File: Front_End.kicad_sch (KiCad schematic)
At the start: 40 parts, among them J6 Conn_01x03, J7 Conn_01x03, J8 Conn_01x03, J9 Conn_01x03

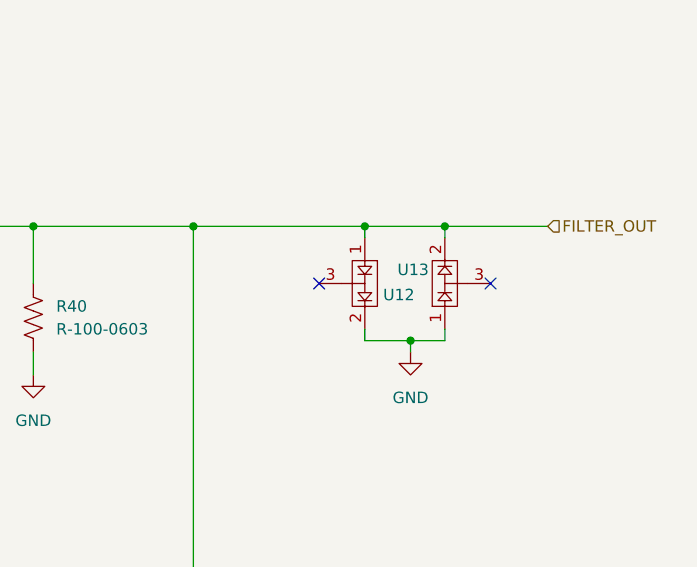
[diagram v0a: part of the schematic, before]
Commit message: Bring over ringof/dev: design + 3D + mechanical/viewer + CI (#58)
* throwaway: exercise design -> dev pipeline (safe to delete)

* Bring over ringof/dev (tranche 2, stage 1): design, library, 3D, board CI & docs

* Bring over ringof/dev (tranche 2, stage 2): mechanical enclosure + 3D viewer

* run_checks: hard-fail the 3D-model check regardless of ENFORCE

* Improved 3D viewer (#59)

* mechanical: give the end plates a Blue soldermask stackup

The end-plate PCBs had no physical stackup, so KiCad exported them with the
default green soldermask. Add a 2-layer stackup with front/back mask set to the
named "Blue" preset, summing to the existing 1.6 mm so board thickness / fit is
unchanged. This makes the plates export blue-dominant so the viewer's soldermask
recolour treats them the same as the main board.

* feat(viewer): part toggles, upright orientation, Turn Island navy, even lighting

Grow the mechanical fit-check viewer into an interactive, correctly-coloured one:

- Part toggles: show/hide enclosure, main board, front/rear end plate. Rebuilt on
  pinned three.js r148 (model-viewer has no per-node visibility API); a checkbox
  flips object.visible on each part's prefixed nodes. Libraries inlined via a
  runtime import map -- no bundler, fully offline.
- Upright orientation (180 deg roll), click-to-set-pivot, and a header showing the
  git hash and branch as links (new --repo-url, fed from the CI environment).
- Board colour: assemble_glb recolours the blue soldermask to the Turn Island navy
  (KiCad's "Blue" preset exports a brighter cornflower); detection targets only the
  matte, blue-dominant mask material. The material is identical on every face, so
  the viewer lighting is set to an orientation-independent rig (soft key + strong
  ambient + damped environment) so every face reads the same navy.
- Checkbox reload-sync: autocomplete="off" + re-apply each box's state on load so
  the model always matches the checkboxes after a refresh.

Colour is applied downstr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
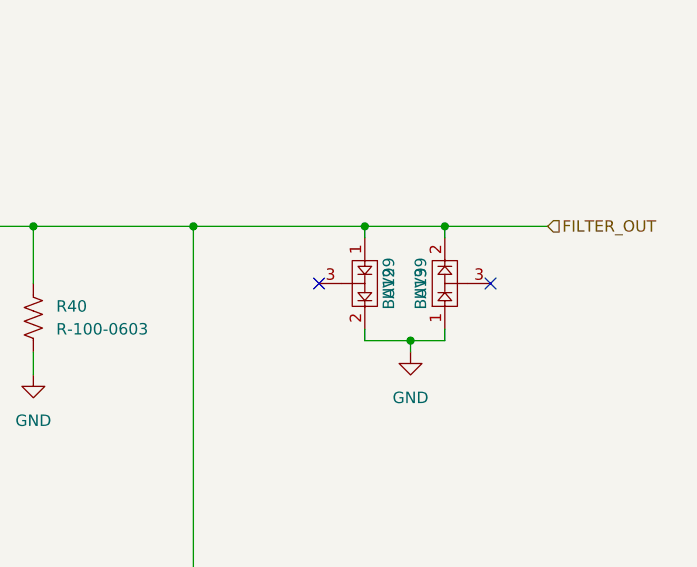
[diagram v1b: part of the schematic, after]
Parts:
- C48, C49, C50, C53, C54, C55, C56, C58, C59, C61: footprint TIS_Footprints:C_0603 -> Library:C_0603
- C51, C52, C57, C60: footprint TIS_Footprints:PAD_0603 -> Library:C_0603
- J6, J7, J8, J9: footprint TIS_Footprints:Pin_Header_Straight_1x03_Pitch2.54mm -> Library:Pin_Header_Straight_1x03_Pitch2.54mm
- L10, L11: footprint TIS_Footprints:Murata2U -> Library:Murata2U; LCSC Part # C2044072 -> C703706
- L12, L13, L14, L8, L9: footprint TIS_Footprints:Murata2U -> Library:Murata2U
- R28, R29, R30, R31, R32, R33, R34, R35, R36, R37, R38, R39, R40: footprint TIS_Footprints:PAD_0603 -> Library:PAD_0603
- U12, U13: value (none) -> BAV99; footprint TIS_Footprints:SOT-23 -> Library:SOT-23
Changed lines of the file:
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@@
 			)
 		)
-		(property "Footprint" "TIS_Footprints:PAD_0603"
+		(property "Footprint" "Library:PAD_0603"
 			(at 117.856 65.024 90)
 			(hide yes)
@@
 			)
 		)
-		(property "Footprint" "TIS_Footprints:PAD_0603"
+		(property "Footprint" "Library:C_0603"
 			(at 60.96 99.06 0)
 			(hide yes)
@@
 			)
 		)
-		(property "Footprint" "TIS_Footprints:Pin_Header_Straight_1x03_Pitch2.54mm"
+		(property "Footprint" "Library:Pin_Header_Straight_1x03_Pitch2.54mm"
 			(at 51.181 21.336 0)
 			(hide yes)
@@
 			)
 		)
-		(property "Footprint" "TIS_Footprints:PAD_0603"
+		(property "Footprint" "Library:PAD_0603"
 			(at 77.216 65.024 90)
 			(hide yes)
@@
 			)
 		)
-		(property "Footprint" "TIS_Footprints:C_0603"
+		(property "Footprint" "Library:C_0603"
 			(at 96.774 135.382 0)
 			(hide yes)
@@
 			)
 		)
-		(property "Footprint" "TIS_Footprints:Murata2U"
+		(property "Footprint" "Library:Murata2U"
 			(at 64.77 111.76 0)
 			(hide yes)
@@
 			)
 		)
-		(property "Footprint" "TIS_Footprints:Murata2U"
+		(property "Footprint" "Library:Murata2U"
 			(at 170.18 111.76 0)
 			(hide yes)
@@
 			)
 		)
-		(property "Footprint" "TIS_Footprints:C_0603"
+		(property "Footprint" "Library:C_0603"
 			(at 115.824 135.382 0)
 			(hide yes)
@@
 			)
 		)
-		(property "Footprint" "TIS_Footprints:C_0603"
+		(property "Footprint" "Library:C_0603"
 			(at 52.324 135.382 0)
 			(hide yes)
@@
 			)
 		)
-		(property "Footprint" "TIS_Footprints:PAD_0603"
+		(property "Footprint" "Library:PAD_0603"
 			(at 124.714 57.404 90)
 			(hide yes)
@@
 			)
 		)
-		(property "Footprint" "TIS_Footprints:PAD_0603"
+		(property "Footprint" "Library:PAD_0603"
 			(at 54.864 157.734 90)
 			(hide yes)
@@
 			)
 		)
-		(property "Footprint" "TIS_Footprints:PAD_0603"
+		(property "Footprint" "Library:PAD_0603"
 			(at 76.454 48.514 90)
 			(hide yes)
@@
 		)
 		(property "LCSC Part #" "C22962"
-			(at 76.2 49.53 0)
+			(at 76.2 49.53 90)
 			(hide yes)
 			(show_name no)
@@
 			)
 		)
-		(property "Footprint" "TIS_Footprints:PAD_0603"
+		(property "Footprint" "Library:PAD_0603"
 			(at 81.534 157.734 90)
 			(hide yes)
@@
 			)
 		)
-		(property "Footprint" "TIS_Footprints:C_0603"
+		(property "Footprint" "Library:C_0603"
 			(at 87.122 114.046 0)
 			(hide yes)
@@
 			)
 		)
-		(property "Footprint" "TIS_Footprints:Pin_Header_Straight_1x03_Pitch2.54mm"
+		(property "Footprint" "Library:Pin_Header_Straight_1x03_Pitch2.54mm"
 			(at 188.849 98.806 0)
 			(hide yes)
@@
 			)
 		)
-		(property "Footprint" "TIS_Footprints:PAD_0603"
+		(property "Footprint" "Library:C_0603"
 			(at 113.03 27.94 0)
 			(hide yes)
@@
 			)
 		)
-		(property "Footprint" "TIS_Footprints:C_0603"
+		(property "Footprint" "Library:C_0603"
 			(at 75.184 135.382 0)
 			(hide yes)
@@
 			)
 		)
-		(property "Footprint" "TIS_Footprints:PAD_0603"
+		(property "Footprint" "Library:PAD_0603"
 			(at 42.926 165.354 90)
 			(hide yes)
@@
 			)
 		)
-		(property "Footprint" "TIS_Footprints:Murata2U"
+		(property "Footprint" "Library:Murata2U"
 			(at 86.36 111.76 0)
 			(hide yes)
@@
 			)
 		)
-		(property "LCSC Part #" "C2044072"
+		(property "LCSC Part #" "C703706"
 			(at 86.487 113.538 0)
 			(hide yes)
@@
 		(dnp no)
 		(property "Reference" "U12"
-			(at 245.872 114.3 90)
+			(at 246.507 113.03 0)
 			(show_name no)
 			(do_not_autoplace no)
@@
 					(size 1.27 1.27)
 				)
-				(justify left)
 			)
 		)
-		(property "Value" ""
-			(at 246.38 114.3635 90)
+		(property "Value" "BAV99"
+			(at 246.507 113.03 0)
 			(show_name no)
 			(do_not_autoplace no)
@@
 					(size 1.27 1.27)
 				)
-				(justify left)
 			)
 		)
-		(property "Footprint" "TIS_Footprints:SOT-23"
+		(property "Footprint" "Library:SOT-23"
 			(at 248.412 112.903 0)
 			(hide yes)
@@
 			)
 		)
-		(property "Footprint" "TIS_Footprints:C_0603"
+		(property "Footprint" "Library:C_0603"
 			(at 33.782 48.006 0)
 			(hide yes)
@@
 		(dnp no)
 		(property "Reference" "U13"
-			(at 250.952 111.506 90)
+			(at 250.063 113.03 0)
 			(show_name no)
 			(do_not_autoplace no)
@@
 					(size 1.27 1.27)
 				)
-				(justify left)
 			)
 		)
-		(property "Value" ""
-			(at 250.19 114.2365 90)
+		(property "Value" "BAV99"
+			(at 250.063 113.03 0)
 			(show_name no)
 			(do_not_autoplace no)
@@
 					(size 1.27 1.27)
 				)
-				(justify left)
 			)
 		)
-		(property "Footprint" "TIS_Footprints:SOT-23"
+		(property "Footprint" "Library:SOT-23"
 			(at 248.158 113.157 0)
 			(hide yes)
@@
 			)
 		)
-		(property "Footprint" "TIS_Footprints:Pin_Header_Straight_1x03_Pitch2.54mm"
+		(property "Footprint" "Library:Pin_Header_Straight_1x03_Pitch2.54mm"
 			(at 48.641 98.806 0)
 			(hide yes)
@@
 			)
 		)
-		(property "Footprint" "TIS_Footprints:PAD_0603"
+		(property "Footprint" "Library:PAD_0603"
 			(at 117.094 48.514 90)
 			(hide yes)
@@
 		)
 		(property "LCSC Part #" "C22962"
-			(at 116.84 49.53 0)
+			(at 116.84 49.53 90)
 			(hide yes)
 			(show_name no)
@@
 			)
 		)
-		(property "Footprint" "TIS_Footprints:PAD_0603"
+		(property "Footprint" "Library:PAD_0603"
 			(at 208.026 117.094 90)
 			(hide yes)
@@
 			)
 		)
-		(property "Footprint" "TIS_Footprints:C_0603"
+		(property "Footprint" "Library:C_0603"
 			(at 129.032 114.046 0)
 			(hide yes)
@@
 			)
 		)
-		(property "Footprint" "TIS_Footprints:C_0603"
+		(property "Footprint" "Library:C_0603"
 			(at 35.052 161.036 0)
 			(hide yes)
@@
 			)
 		)
-		(property "Footprint" "TIS_Footprints:C_0603"
+		(property "Footprint" "Library:C_0603"
 			(at 107.442 114.046 0)
 			(hide yes)
@@
 			)
 		)
-		(property "Footprint" "TIS_Footprints:Murata2U"
+		(property "Footprint" "Library:Murata2U"
 			(at 64.77 73.66 0)
 			(hide yes)
@@
 			)
 		)
-		(property "Footprint" "TIS_Footprints:Murata2U"
+		(property "Footprint" "Library:Murata2U"
 			(at 105.41 73.66 0)
 			(hide yes)
@@
 			)
 		)
-		(property "Footprint" "TIS_Footprints:Murata2U"
+		(property "Footprint" "Library:Murata2U"
 			(at 128.27 111.76 0)
 			(hide yes)
@@
 			)
 		)
-		(property "Footprint" "TIS_Footprints:PAD_0603"
+		(property "Footprint" "Library:C_0603"
 			(at 162.56 130.81 0)
 			(hide yes)
@@
 			)
 		)
-		(property "Footprint" "TIS_Footprints:PAD_0603"
+		(property "Footprint" "Library:PAD_0603"
 			(at 109.474 57.404 90)
 			(hide yes)
@@
 			)
 		)
-		(property "Footprint" "TIS_Footprints:Murata2U"
+		(property "Footprint" "Library:Murata2U"
 			(at 106.68 111.76 0)
 			(hide yes)
@@
 			)
 		)
-		(property "LCSC Part #" "C2044072"
+		(property "LCSC Part #" "C703706"
 			(at 106.807 113.538 0)
 			(hide yes)
@@
 			)
 		)
-		(property "Footprint" "TIS_Footprints:PAD_0603"
+		(property "Footprint" "Library:PAD_0603"
 			(at 68.834 57.404 90)
 			(hide yes)
@@
 			)
 		)
-		(property "Footprint" "TIS_Footprints:PAD_0603"
+		(property "Footprint" "Library:PAD_0603"
 			(at 84.074 57.404 90)
 			(hide yes)
@@
 			)
 		)
-		(property "Footprint" "TIS_Footprints:PAD_0603"
+		(property "Footprint" "Library:PAD_0603"
 			(at 68.326 165.354 90)
 			(hide yes)
@@
 			)
 		)
-		(property "Footprint" "TIS_Footprints:C_0603"
+		(property "Footprint" "Library:C_0603"
 			(at 180.594 134.112 0)
 			(hide yes)
@@
 			)
 		)
-		(property "Footprint" "TIS_Footprints:PAD_0603"
+		(property "Footprint" "Library:C_0603"
 			(at 72.39 27.94 0)
 			(hide yes)
@@
 			)
 		)
-		(property "Footprint" "TIS_Footprints:Pin_Header_Straight_1x03_Pitch2.54mm"
+		(property "Footprint" "Library:Pin_Header_Straight_1x03_Pitch2.54mm"
 			(at 145.669 21.336 0)
 			(hide yes)
